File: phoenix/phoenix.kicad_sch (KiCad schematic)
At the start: 15 parts, among them J1 JST_B4B_XH_A, U1 Teensy4.1, U2 BMP280, U3 LIS3MDLTR, U4 LSM6DSOXTR

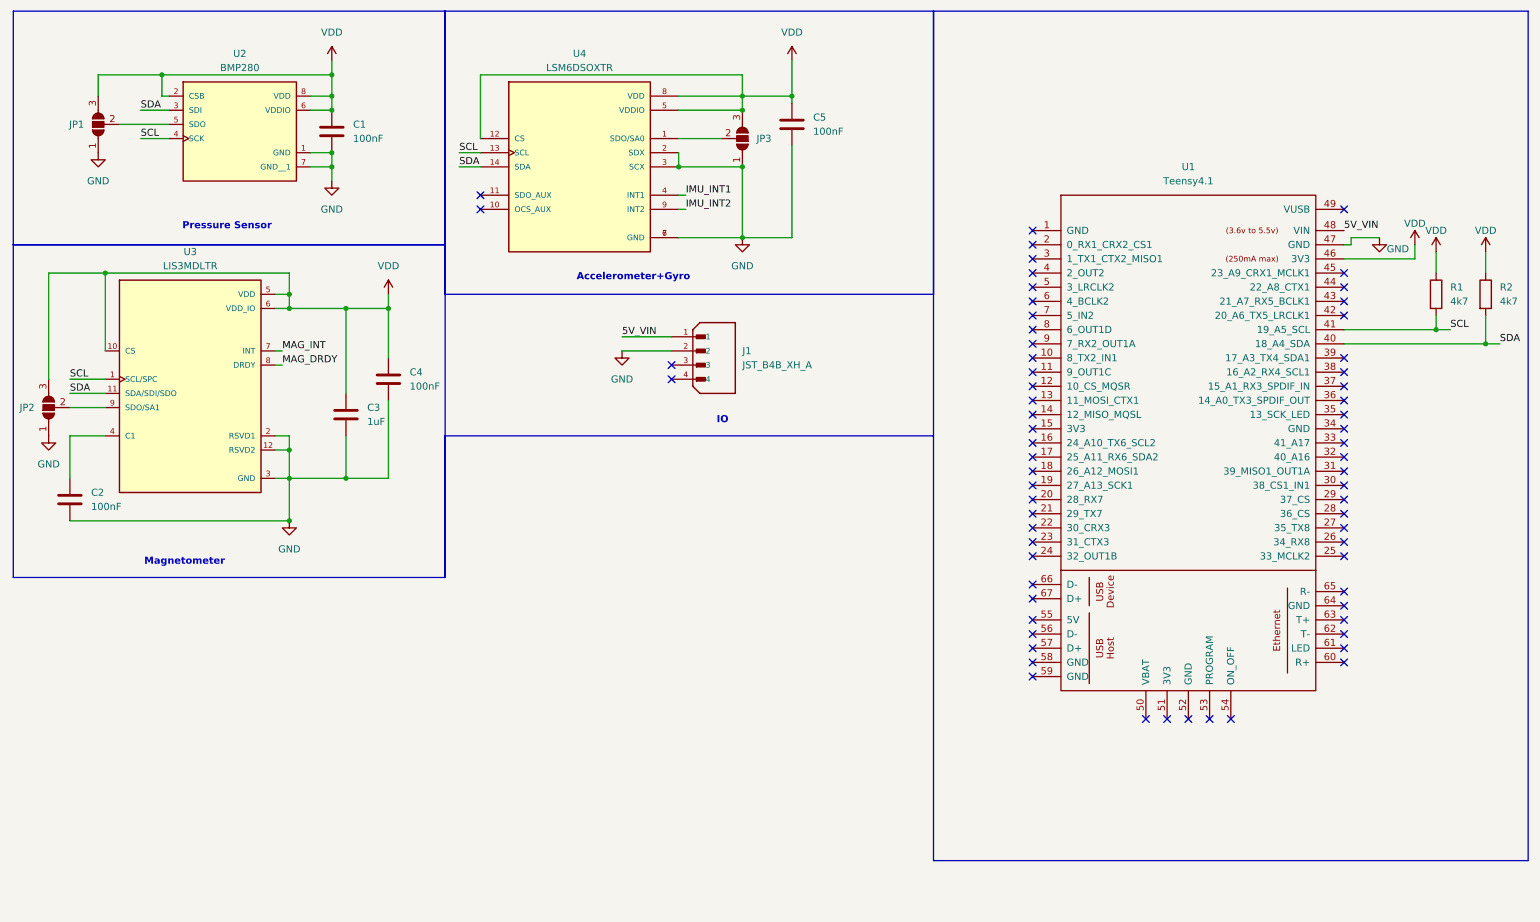
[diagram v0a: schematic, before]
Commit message: Added backup radio and debug LEDs
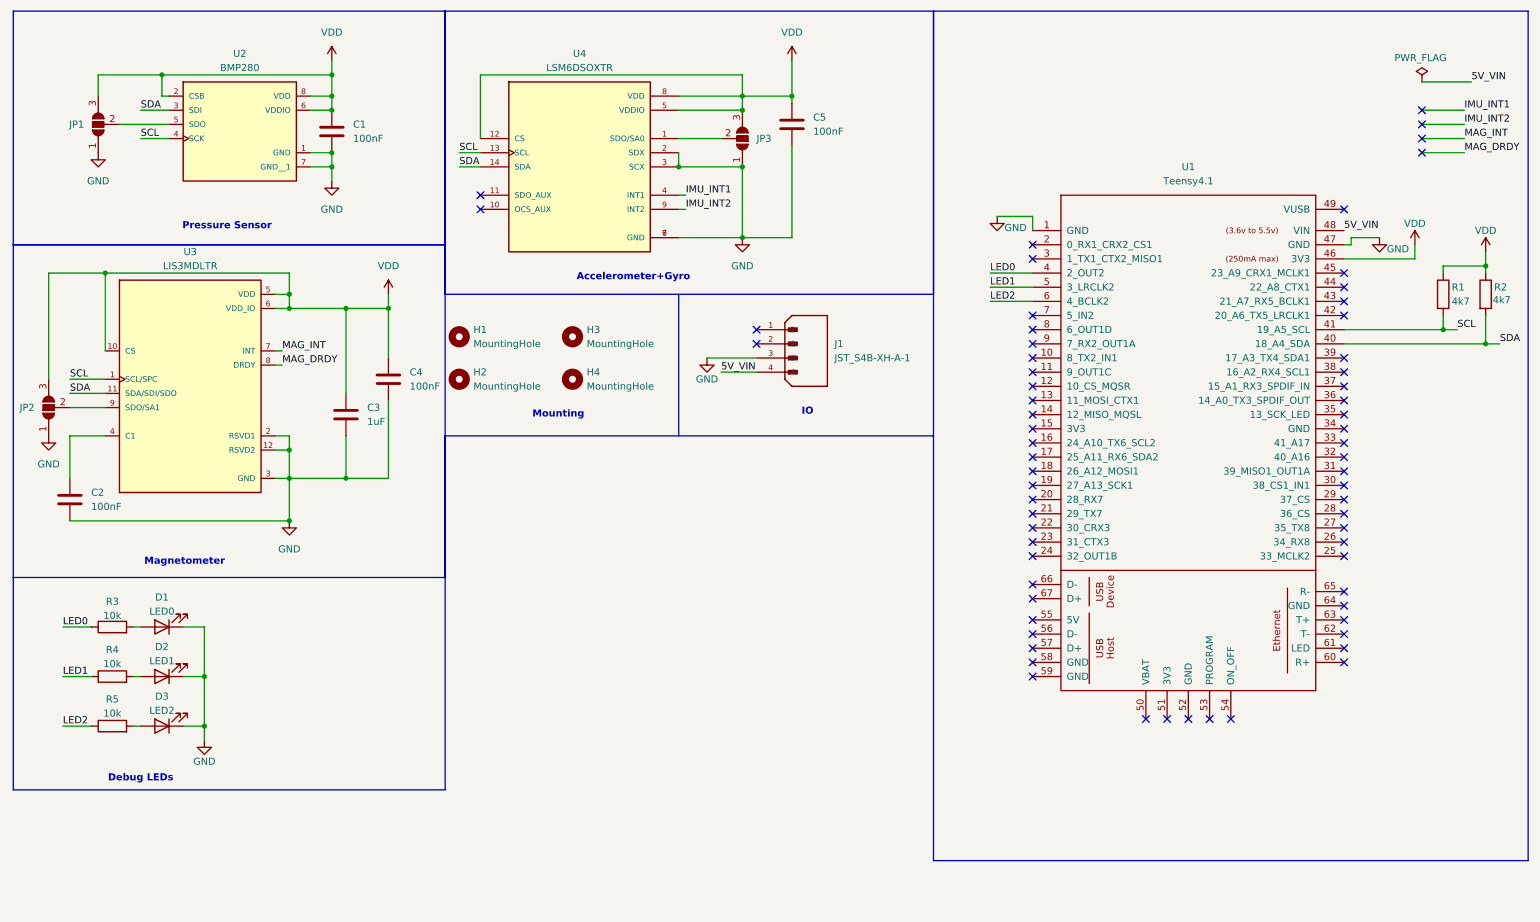
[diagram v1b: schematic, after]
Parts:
- removed J1: JST_B4B_XH_A, custom_library:JST_B4B-XH-A, symbol custom_library:JST_B4B_XH_A
- added D1: LED0, LED_SMD:LED_0603_1608Metric, symbol Device:LED
- added D2: LED1, LED_SMD:LED_0603_1608Metric, symbol Device:LED
- added D3: LED2, LED_SMD:LED_0603_1608Metric, symbol Device:LED
- added H1, H2, H3, H4: MountingHole, MountingHole:MountingHole_3.2mm_M3, symbol Mechanical:MountingHole
- added J1: JST_S4B-XH-A-1, custom_library:JST_S4B-XH-A-1, symbol custom_library:JST_S4B-XH-A-1
- added R3, R4, R5: 10k, Resistor_SMD:R_0805_2012Metric, symbol Device:R
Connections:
- net 5V_VIN: now also J1.4
- net GND: now also U1.1 (GND), D1.1 (K), D2.1 (K), D3.1 (K), J1.3
- net LED0: now reaches U1.4 (2_OUT2)
- net LED0: now also R3.1
- net LED1: now reaches U1.5 (3_LRCLK2)
- net LED1: now also R4.1
- net LED2: now reaches U1.6 (4_BCLK2)
- net LED2: now also R5.1
- new net: D2.2 (A), R4.2
- new net: D3.2 (A), R5.2
- new net: D1.2 (A), R3.2
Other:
- note added: "Debug LEDs"
- note added: "Mounting"
- moved on the sheet: R1

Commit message: Add SPI sd card
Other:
- added sheet MCU (mcu.kicad_sch)
- added sheet SD Card (sdcard.kicad_sch)
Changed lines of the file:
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@@
 	(label "MAG_INT"
 		(at 273.05 35.56 0)
-		(fields_autoplaced yes)
 		(effects
 			(font
@@
 	(label "LED2"
 		(at 187.96 64.77 0)
-		(fields_autoplaced yes)
 		(effects
 			(font
@@
 	(label "MAG_DRDY"
 		(at 273.05 38.1 0)
-		(fields_autoplaced yes)
 		(effects
 			(font
@@
 	(label "SCL"
 		(at 92.71 38.1 0)
-		(fields_autoplaced yes)
 		(effects
 			(font
@@
 	(label "SCL"
 		(at 22.86 78.74 0)
-		(fields_autoplaced yes)
 		(effects
 			(font
@@
 	(label "SCL"
 		(at 271.78 69.85 0)
-		(fields_autoplaced yes)
 		(effects
 			(font
@@
 	(label "5V_VIN"
 		(at 139.7 77.47 0)
-		(fields_autoplaced yes)
 		(effects
 			(font
@@
 	(label "SDA"
 		(at 92.71 40.64 0)
-		(fields_autoplaced yes)
 		(effects
 			(font
@@
 	(label "IMU_INT1"
 		(at 273.05 30.48 0)
-		(fields_autoplaced yes)
 		(effects
 			(font
@@
 	(label "IMU_INT2"
 		(at 133.35 48.26 0)
-		(fields_autoplaced yes)
 		(effects
 			(font
@@
 	(label "5V_VIN"
 		(at 274.32 25.4 0)
-		(fields_autoplaced yes)
 		(effects
 			(font
@@
 	(label "SCL"
 		(at 35.56 35.56 0)
-		(fields_autoplaced yes)
 		(effects
 			(font
@@
 	(label "5V_VIN"
 		(at 251.46 52.07 0)
-		(fields_autoplaced yes)
 		(effects
 			(font
@@
 	(label "LED0"
 		(at 21.59 123.19 0)
-		(fields_autoplaced yes)
 		(effects
 			(font
@@
 	(label "LED0"
 		(at 187.96 59.69 0)
-		(fields_autoplaced yes)
 		(effects
 			(font
@@
 	(label "MAG_DRDY"
 		(at 60.96 76.2 0)
-		(fields_autoplaced yes)
 		(effects
 			(font
@@
 	(label "LED1"
 		(at 21.59 132.08 0)
-		(fields_autoplaced yes)
 		(effects
 			(font
@@
 	(label "SDA"
 		(at 279.4 72.39 0)
-		(fields_autoplaced yes)
 		(effects
 			(font
@@
 	(label "SDA"
 		(at 22.86 81.28 0)
-		(fields_autoplaced yes)
 		(effects
 			(font
@@
 	(label "LED2"
 		(at 21.59 140.97 0)
-		(fields_autoplaced yes)
 		(effects
 			(font
@@
 	(label "IMU_INT2"
 		(at 273.05 33.02 0)
-		(fields_autoplaced yes)
 		(effects
 			(font
@@
 	(label "SDA"
 		(at 35.56 30.48 0)
-		(fields_autoplaced yes)
 		(effects
 			(font
@@
 	(label "LED1"
 		(at 187.96 62.23 0)
-		(fields_autoplaced yes)
 		(effects
 			(font
@@
 	(label "MAG_INT"
 		(at 60.96 73.66 0)
-		(fields_autoplaced yes)
 		(effects
 			(font
@@
 	(label "IMU_INT1"
 		(at 133.35 45.72 0)
-		(fields_autoplaced yes)
 		(effects
 			(font
@@
 				)
 			)
+		)
+	)
+	(sheet
+		(at 111.76 123.19)
+		(size 46.99 27.94)
+		(fields_autoplaced yes)
+		(stroke
+			(width 0.1524)
+			(type solid)
+		)
+		(fill
+			(color 0 0 0 0.0000)
+		)
+		(property "Sheetname" "MCU"
+			(at 111.76 122.4784 0)
+			(effects
+				(font
+					(size 1.27 1.27)
+				)
+				(justify left bottom)
+			)
+		)
+		(property "Sheetfile" "mcu.kicad_sch"
+			(at 111.76 151.7146 0)
+			(effects
+				(font
+					(size 1.27 1.27)
+				)
+				(justify left top)
+			)
+		)
+		(instances
+			(project "phoenix"
+				(path "/8a6ea20b-142f-494e-b68b-0e8978f936c5"
+					(page "2")
+				)
+			)
+		)
+	)
+	(sheet
+		(at 107.95 160.02)
+		(size 27.94 11.43)
+		(fields_autoplaced yes)
+		(stroke
+			(width 0.1524)
+			(type solid)
+		)
+		(fill
+			(color 0 0 0 0.0000)
+		)
+		(property "Sheetname" "SD Card"
+			(at 107.95 159.3084 0)
+			(effects
+				(font
+					(size 1.27 1.27)
+				)
+				(justify left bottom)
+			)
+		)
+		(property "Sheetfile" "sdcard.kicad_sch"
+			(at 107.95 172.0346 0)
+			(effects
+				(font
+					(size 1.27 1.27)
+				)
+				(justify left top)
+			)
+		)
+		(pin "SPI{nCS,MOSI,SCLK,MISO}" bidirectional
+			(at 135.89 166.37 0)
+			(effects
+				(font
+					(size 1.27 1.27)
+				)
+				(justify right)
+			)
+		)
+		(instances
+			(project "phoenix"
+				(path "/8a6ea20b-142f-494e-b68b-0e8978f936c5"
+					(page "3")
+				)
+			)

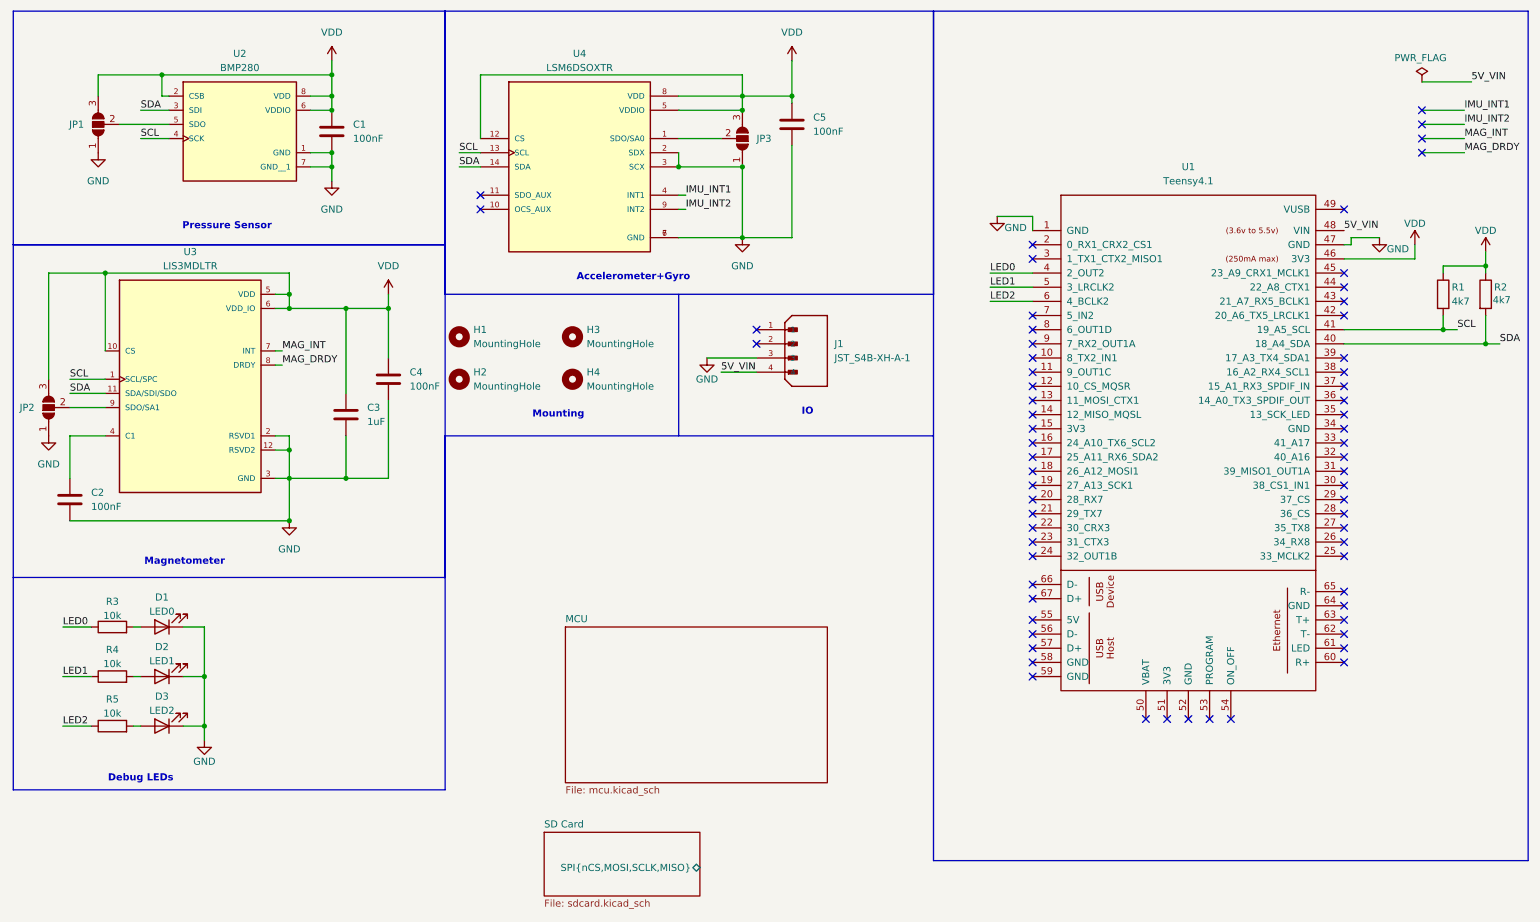
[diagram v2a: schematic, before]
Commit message: Finished schematics and almost done layouts of LC26 PCBs
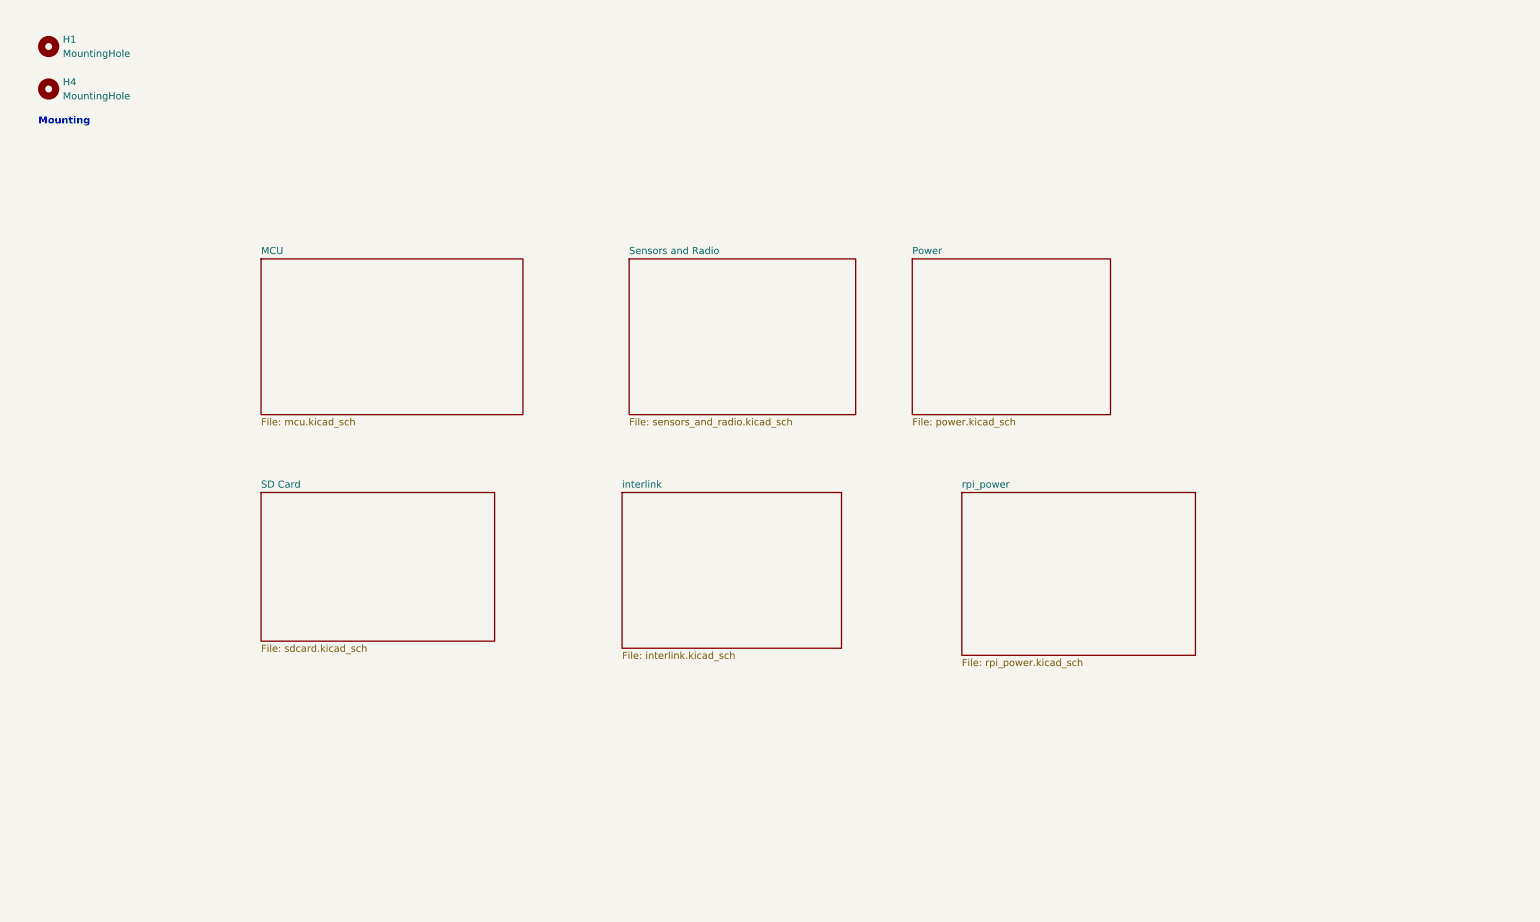
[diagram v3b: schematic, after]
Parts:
- removed C1, C2, C4, C5: 100nF, Capacitor_SMD:C_0805_2012Metric, symbol Device:C
- removed C3: 1uF, Capacitor_SMD:C_0805_2012Metric, symbol Device:C
- removed D1: LED0, LED_SMD:LED_0603_1608Metric, symbol Device:LED
- removed D2: LED1, LED_SMD:LED_0603_1608Metric, symbol Device:LED
- removed D3: LED2, LED_SMD:LED_0603_1608Metric, symbol Device:LED
- removed H2, H3: MountingHole, MountingHole:MountingHole_3.2mm_M3, symbol Mechanical:MountingHole
- removed J1: JST_S4B-XH-A-1, custom_library:JST_S4B-XH-A-1, symbol custom_library:JST_S4B-XH-A-1
- removed JP1, JP2, JP3: SolderJumper_3_Open, Jumper:SolderJumper-3_P1.3mm_Open_Pad1.0x1.5mm_NumberLabels, symbol Jumper:SolderJumper_3_Open
- removed R1, R2: 4k7, Resistor_SMD:R_0805_2012Metric, symbol Device:R
- removed R3, R4, R5: 10k, Resistor_SMD:R_0805_2012Metric, symbol Device:R
- removed U1: Teensy4.1, custom_library:Teensy41, symbol custom_library:Teensy4.1
- removed U2: BMP280, custom_library:BMP280, symbol custom_library:BMP280
- removed U3: LIS3MDLTR, custom_library:LIS3MDLTR, symbol custom_library:LIS3MDLTR
- removed U4: LSM6DSOXTR, custom_library:LSM6DSOXTR, symbol custom_library:LSM6DSOXTR
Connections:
- no-connect marks 66 -> 0
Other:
- added sheet Power (power.kicad_sch)
- added sheet Sensors and Radio (sensors_and_radio.kicad_sch)
- added sheet interlink (interlink.kicad_sch)
- added sheet rpi_power (rpi_power.kicad_sch)
- sheet SD Card ports: added none; removed SPI{nCS,MOSI,SCLK,MISO}
- note removed: "Accelerometer+Gyro"
- note removed: "Debug LEDs"
- note removed: "IO"
- note removed: "Magnetometer"
- note removed: "Pressure Sensor"
- moved on the sheet: H1, H4
